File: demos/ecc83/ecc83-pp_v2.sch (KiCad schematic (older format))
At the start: 11 parts, among them P1 IN, P2 OUT, P3 POWER, P4 CONN_2, U1 ECC83

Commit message: Some demo files updated.
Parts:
- U1: value ECC83 -> ECC81_83
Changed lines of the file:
@@
-EESchema Schematic File Version 2  date 30/12/2010 18:27:52
-LIBS:power
-LIBS:device
-LIBS:valves
-LIBS:conn
-LIBS:linear
-LIBS:regul
-LIBS:74xx
-LIBS:cmos4000
-LIBS:adc-dac
-LIBS:memory
-LIBS:xilinx
-LIBS:special
-LIBS:microcontrollers
-LIBS:microchip
-LIBS:analog_switches
-LIBS:motorola
-LIBS:intel
-LIBS:audio
-LIBS:interface
-LIBS:digital-audio
-LIBS:philips
-LIBS:display
-LIBS:cypress
-LIBS:siliconi
-LIBS:contrib
-LIBS:ecc83-pp_v2-cache
-EELAYER 25  0
+EESchema Schematic File Version 2
+LIBS:power,device,valves,conn,linear,regul,74xx,cmos4000,adc-dac,memory,xilinx,special,microcontrollers,microchip,analog_switches,motorola,intel,audio,interface,digital-audio,philips,display,cypress,siliconi,contrib
+EELAYER 23  0
 EELAYER END
 $Descr A4 11700 8267
 Sheet 1 1
 Title "ECC Push-Pull"
-Date "30 dec 2010"
+Date "11 dec 2006"
 Rev "0.1"
 Comp ""
@@
 Wire Wire Line
 	5750 3850 5750 4050
+Connection ~ 4450 4500
 Wire Wire Line
 	4450 5400 4450 4450
@@
 U 3 1 48B4F266
 P 9950 5700
-F 0 "U1" H 10080 6010 50  0000 C CNN
-F 1 "ECC83" H 10300 5400 50  0000 C CNN
-F 2 "VALVE-NOVAL_P" H 10220 5300 50  0001 C CNN
+F 0 "U1" H 10080 6010 50  0000 C C
+F 1 "ECC81_83" H 10300 5400 50  0000 C C
+F 2 "VALVE-NOVAL_P" H 10220 5300 50  0001 C C
 	3    9950 5700
 	1    0    0    -1
@@
 U 2 1 48B4F263
 P 4950 4450
-F 0 "U1" H 5080 4760 50  0000 C CNN
-F 1 "ECC83" H 5150 4100 50  0000 C CNN
-F 2 "VALVE-NOVAL_P" H 5220 4050 50  0001 C CNN
+F 0 "U1" H 5080 4760 50  0000 C C
+F 1 "ECC83" H 5150 4100 50  0000 C C
+F 2 "VALVE-NOVAL_P" H 5220 4050 50  0001 C C
 	2    4950 4450
 	1    0    0    -1
@@
 U 1 1 48B4F256
 P 5750 4450
-F 0 "U1" H 5880 4760 50  0000 C CNN
-F 1 "ECC83" H 5500 4150 50  0000 C CNN
-F 2 "VALVE-NOVAL_P" H 6020 4050 50  0001 C CNN
+F 0 "U1" H 5880 4760 50  0000 C C
+F 1 "ECC83" H 5500 4150 50  0000 C C
+F 2 "VALVE-NOVAL_P" H 6020 4050 50  0001 C C
 	1    5750 4450
 	-1   0    0    -1
@@
 U 1 1 457DBAF8
 P 6950 5150
-F 0 "#PWR01" H 6950 5150 30  0001 C CNN
-F 1 "GND" H 6950 5080 30  0001 C CNN
+F 0 "#PWR01" H 6950 5150 30  0001 C C
+F 1 "GND" H 6950 5080 30  0001 C C
 	1    6950 5150
 	1    0    0    -1
@@
 U 1 1 457DBAF5
 P 6700 5900
-F 0 "#PWR02" H 6700 5900 30  0001 C CNN
-F 1 "GND" H 6700 5830 30  0001 C CNN
+F 0 "#PWR02" H 6700 5900 30  0001 C C
+F 1 "GND" H 6700 5830 30  0001 C C
 	1    6700 5900
 	1    0    0    -1
@@
 U 1 1 457DBAF1
 P 4850 5900
-F 0 "#PWR03" H 4850 5900 30  0001 C CNN
-F 1 "GND" H 4850 5830 30  0001 C CNN
+F 0 "#PWR03" H 4850 5900 30  0001 C C
+F 1 "GND" H 4850 5830 30  0001 C C
 	1    4850 5900
 	1    0    0    -1
@@
 U 1 1 457DBAEF
 P 4450 5900
-F 0 "#PWR04" H 4450 5900 30  0001 C CNN
-F 1 "GND" H 4450 5830 30  0001 C CNN
+F 0 "#PWR04" H 4450 5900 30  0001 C C
+F 1 "GND" H 4450 5830 30  0001 C C
 	1    4450 5900
 	1    0    0    -1
@@
 U 1 1 457DBAC0
 P 4100 5250
-F 0 "#FLG05" H 4100 5520 30  0001 C CNN
-F 1 "PWR_FLAG" H 4100 5480 30  0000 C CNN
+F 0 "#FLG05" H 4100 5520 30  0001 C C
+F 1 "PWR_FLAG" H 4100 5480 30  0000 C C
 	1    4100 5250
 	0    -1   -1   0
@@
 U 1 1 456A8ACC
 P 9950 6700
-F 0 "P4" V 9900 6700 40  0000 C CNN
-F 1 "CONN_2" V 10000 6700 40  0000 C CNN
+F 0 "P4" V 9900 6700 40  0000 C C
+F 1 "CONN_2" V 10000 6700 40  0000 C C
 	1    9950 6700
 	0    1    1    0
@@
 U 1 1 4549F4BE
 P 6700 4050
-F 0 "C1" H 6750 4150 50  0000 L CNN
-F 1 "10uF" H 6450 4150 50  0000 L CNN
+F 0 "C1" H 6750 4150 50  0000 L C
+F 1 "10uF" H 6450 4150 50  0000 L C
 	1    6700 4050
 	1    0    0    -1
@@
 U 1 1 4549F4B9
 P 4150 5300
-F 0 "#PWR06" H 4150 5300 30  0001 C CNN
-F 1 "GND" H 4150 5230 30  0001 C CNN
+F 0 "#PWR06" H 4150 5300 30  0001 C C
+F 1 "GND" H 4150 5230 30  0001 C C
 	1    4150 5300
 	1    0    0    -1
@@
 U 1 1 4549F4B3
 P 6950 4350
-F 0 "#PWR07" H 6950 4350 30  0001 C CNN
-F 1 "GND" H 6950 4280 30  0001 C CNN
+F 0 "#PWR07" H 6950 4350 30  0001 C C
+F 1 "GND" H 6950 4280 30  0001 C C
 	1    6950 4350
 	1    0    0    -1
@@
 U 1 1 4549F4A5
 P 7300 3950
-F 0 "P3" V 7250 3950 40  0000 C CNN
-F 1 "POWER" V 7350 3950 40  0000 C CNN
+F 0 "P3" V 7250 3950 40  0000 C C
+F 1 "POWER" V 7350 3950 40  0000 C C
 	1    7300 3950
 	1    0    0    -1
@@
 U 1 1 4549F46C
 P 7300 4900
-F 0 "P2" V 7250 4900 40  0000 C CNN
-F 1 "OUT" V 7350 4900 40  0000 C CNN
+F 0 "P2" V 7250 4900 40  0000 C C
+F 1 "OUT" V 7350 4900 40  0000 C C
 	1    7300 4900
 	1    0    0    -1
@@
 U 1 1 4549F464
 P 3800 4900
-F 0 "P1" V 3750 4900 40  0000 C CNN
-F 1 "IN" V 3850 4900 40  0000 C CNN
+F 0 "P1" V 3750 4900 40  0000 C C
+F 1 "IN" V 3850 4900 40  0000 C C
 	1    3800 4900
 	-1   0    0    1
@@
 U 1 1 4549F3BE
 P 6500 4800
-F 0 "C2" H 6550 4900 50  0000 L CNN
-F 1 "680nF" H 6550 4700 50  0000 L CNN
+F 0 "C2" H 6550 4900 50  0000 L C
+F 1 "680nF" H 6550 4700 50  0000 L C
 	1    6500 4800
 	0    1    1    0
@@
 U 1 1 4549F3AD
 P 6700 5650
-F 0 "R3" V 6780 5650 50  0000 C CNN
-F 1 "100K" V 6700 5650 50  0000 C CNN
+F 0 "R3" V 6780 5650 50  0000 C C
+F 1 "100K" V 6700 5650 50  0000 C C
 	1    6700 5650
 	1    0    0    -1
@@
 U 1 1 4549F3A2
 P 4450 5650
-F 0 "R4" V 4530 5650 50  0000 C CNN
-F 1 "47K" V 4450 5650 50  0000 C CNN
+F 0 "R4" V 4530 5650 50  0000 C C
+F 1 "47K" V 4450 5650 50  0000 C C
 	1    4450 5650
 	1    0    0    -1
@@
 U 1 1 4549F39D
 P 4850 5650
-F 0 "R2" V 4930 5650 50  0000 C CNN
-F 1 "1.5K" V 4850 5650 50  0000 C CNN
+F 0 "R2" V 4930 5650 50  0000 C C
+F 1 "1.5K" V 4850 5650 50  0000 C C
 	1    4850 5650
 	1    0    0    -1
@@
 U 1 1 4549F38A
 P 6300 4250
-F 0 "R1" V 6380 4250 50  0000 C CNN
-F 1 "1.5K" V 6300 4250 50  0000 C CNN
+F 0 "R1" V 6380 4250 50  0000 C C
+F 1 "1.5K" V 6300 4250 50  0000 C C
 	1    6300 4250
 	1    0    0    -1

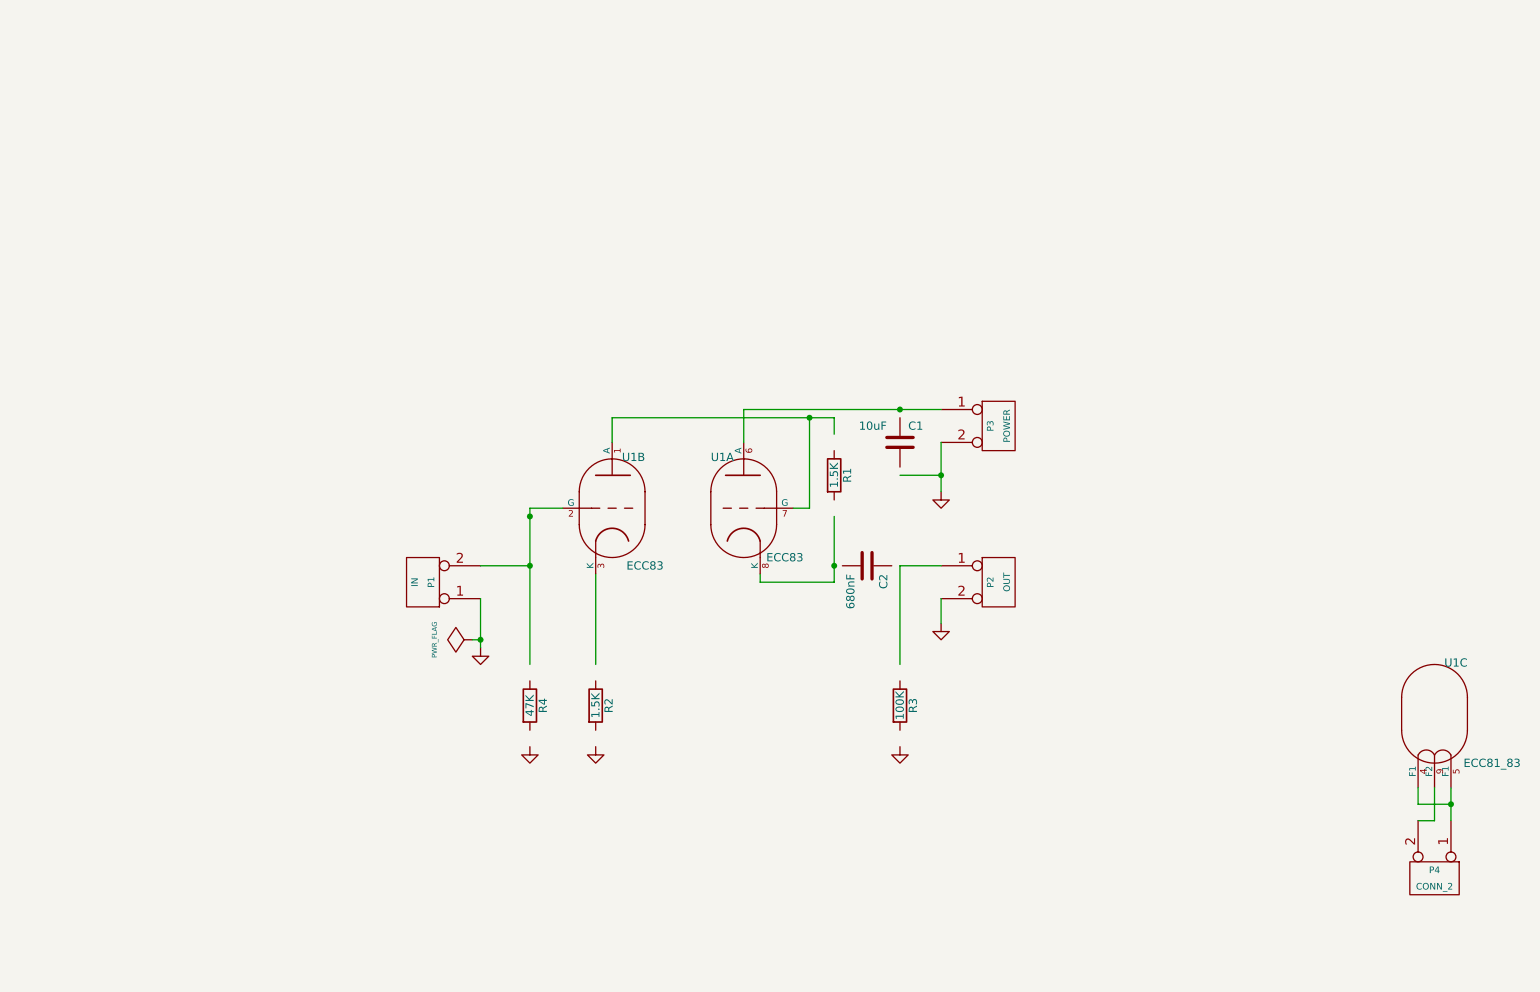
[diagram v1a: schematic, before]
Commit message: Update old demo board files. Minor code cleaning.
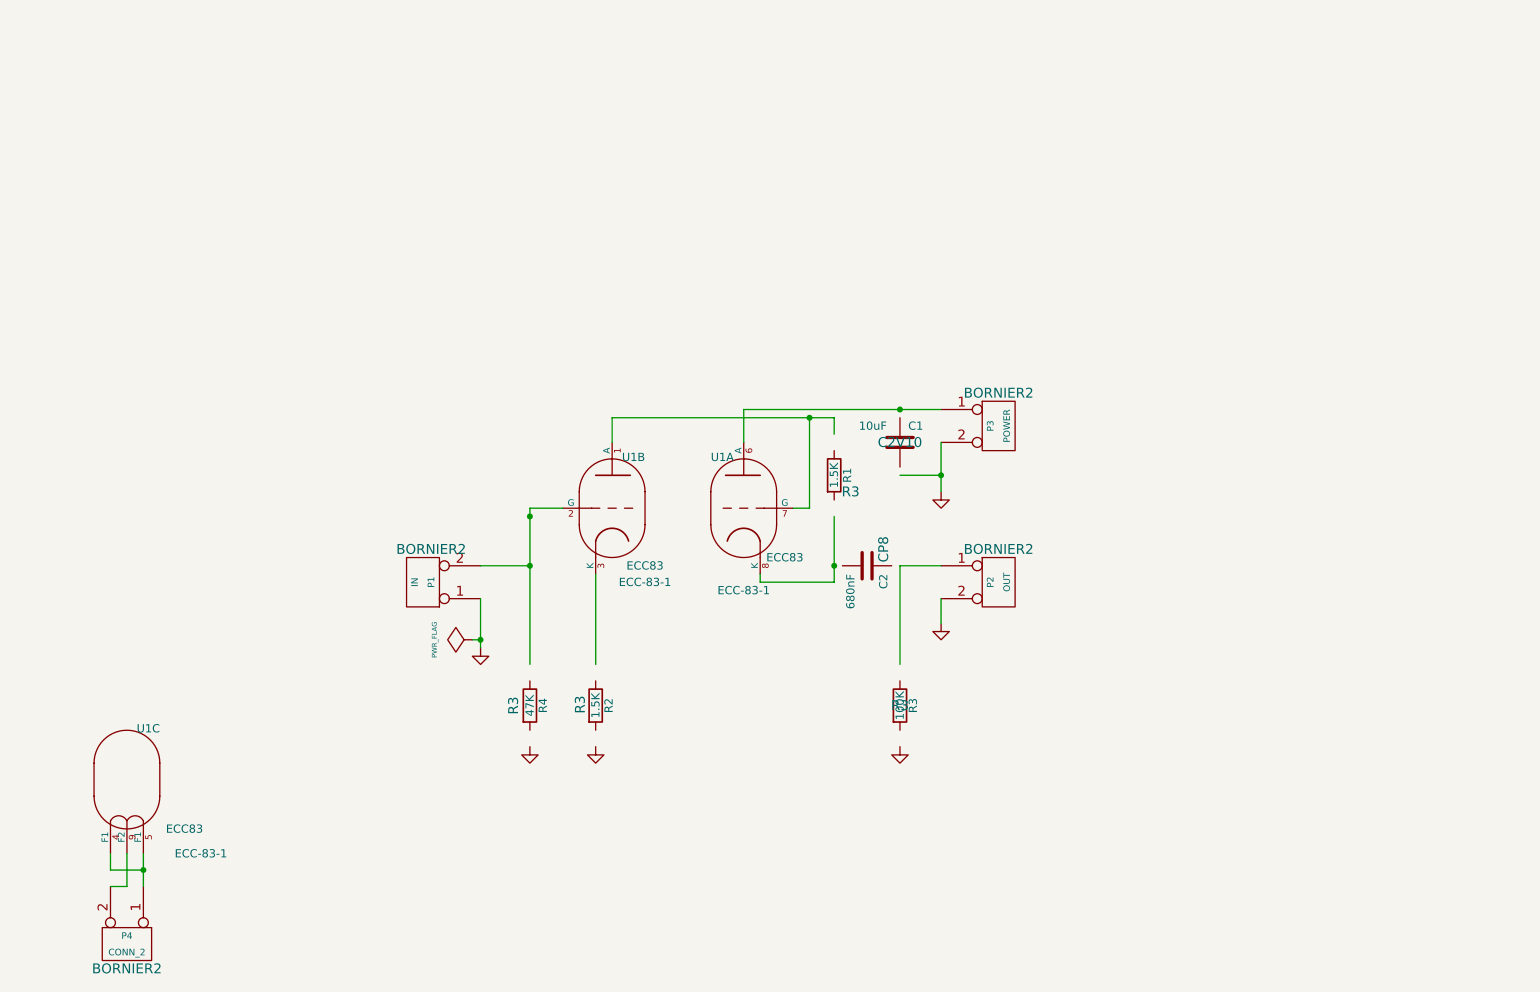
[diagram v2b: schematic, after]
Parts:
- C1: footprint (none) -> C2V10
- C2: footprint (none) -> CP8
- P1, P2, P3, P4: footprint (none) -> BORNIER2
- R1, R2, R3, R4: footprint (none) -> R3
- U1: footprint VALVE-NOVAL_P -> ECC-83-1
- U1: value ECC81_83 -> ECC83; footprint VALVE-NOVAL_P -> ECC-83-1
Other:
- moved on the sheet: P4, U1C
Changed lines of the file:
@@
 EESchema Schematic File Version 2
-LIBS:power,device,valves,conn,linear,regul,74xx,cmos4000,adc-dac,memory,xilinx,special,microcontrollers,microchip,analog_switches,motorola,intel,audio,interface,digital-audio,philips,display,cypress,siliconi,contrib
-EELAYER 23  0
+LIBS:power
+LIBS:device
+LIBS:valves
+LIBS:conn
+LIBS:linear
+LIBS:regul
+LIBS:74xx
+LIBS:cmos4000
+LIBS:adc-dac
+LIBS:memory
+LIBS:xilinx
+LIBS:special
+LIBS:microcontrollers
+LIBS:microchip
+LIBS:analog_switches
+LIBS:motorola
+LIBS:intel
+LIBS:audio
+LIBS:interface
+LIBS:digital-audio
+LIBS:philips
+LIBS:display
+LIBS:cypress
+LIBS:siliconi
+LIBS:contrib
+LIBS:ecc83-pp_v2-cache
+EELAYER 24 0
 EELAYER END
-$Descr A4 11700 8267
+$Descr A4 11693 8268
+encoding utf-8
 Sheet 1 1
 Title "ECC Push-Pull"
@@
 	4450 4450 4650 4450
 Wire Wire Line
-	9850 6350 9950 6350
-Wire Wire Line
-	9950 6350 9950 6150
+	1900 6750 2000 6750
+Wire Wire Line
+	2000 6750 2000 6550
 Wire Wire Line
 	4150 5300 4150 5000
@@
 	6700 4800 6700 5400
 Wire Wire Line
-	10050 6150 10050 6350
-Wire Wire Line
-	10050 6250 9850 6250
-Connection ~ 10050 6250
+	2100 6550 2100 6750
+Wire Wire Line
+	2100 6650 1900 6650
+Connection ~ 2100 6650
 Wire Wire Line
 	4100 5250 4150 5250
 Connection ~ 4150 5250
 Wire Wire Line
-	9850 6250 9850 6150
+	1900 6650 1900 6550
 Wire Wire Line
 	6300 3900 4950 3900
@@
 L ECC83 U1
 U 3 1 48B4F266
-P 9950 5700
-F 0 "U1" H 10080 6010 50  0000 C C
-F 1 "ECC81_83" H 10300 5400 50  0000 C C
-F 2 "VALVE-NOVAL_P" H 10220 5300 50  0001 C C
-	3    9950 5700
+P 2000 6100
+F 0 "U1" H 2130 6410 50  0000 C CNN
+F 1 "ECC83" H 2350 5800 50  0000 C CNN
+F 2 "ECC-83-1" H 2450 5650 50  0000 C CNN
+F 3 "" H 2000 6100 60  0001 C CNN
+	3    2000 6100
 	1    0    0    -1
 $EndComp
@@
 U 2 1 48B4F263
 P 4950 4450
-F 0 "U1" H 5080 4760 50  0000 C C
-F 1 "ECC83" H 5150 4100 50  0000 C C
-F 2 "VALVE-NOVAL_P" H 5220 4050 50  0001 C C
+F 0 "U1" H 5080 4760 50  0000 C CNN
+F 1 "ECC83" H 5150 4100 50  0000 C CNN
+F 2 "ECC-83-1" H 5150 4000 50  0000 C CNN
+F 3 "" H 4950 4450 60  0001 C CNN
 	2    4950 4450
 	1    0    0    -1
@@
 U 1 1 48B4F256
 P 5750 4450
-F 0 "U1" H 5880 4760 50  0000 C C
-F 1 "ECC83" H 5500 4150 50  0000 C C
-F 2 "VALVE-NOVAL_P" H 6020 4050 50  0001 C C
+F 0 "U1" H 5880 4760 50  0000 C CNN
+F 1 "ECC83" H 5500 4150 50  0000 C CNN
+F 2 "ECC-83-1" H 5750 3950 50  0000 C CNN
+F 3 "" H 5750 4450 60  0001 C CNN
 	1    5750 4450
 	-1   0    0    -1
@@
 U 1 1 457DBAF8
 P 6950 5150
-F 0 "#PWR01" H 6950 5150 30  0001 C C
-F 1 "GND" H 6950 5080 30  0001 C C
+F 0 "#PWR01" H 6950 5150 30  0001 C CNN
+F 1 "GND" H 6950 5080 30  0001 C CNN
+F 2 "" H 6950 5150 60  0001 C CNN
+F 3 "" H 6950 5150 60  0001 C CNN
 	1    6950 5150
 	1    0    0    -1
@@
 U 1 1 457DBAF5
 P 6700 5900
-F 0 "#PWR02" H 6700 5900 30  0001 C C
-F 1 "GND" H 6700 5830 30  0001 C C
+F 0 "#PWR02" H 6700 5900 30  0001 C CNN
+F 1 "GND" H 6700 5830 30  0001 C CNN
+F 2 "" H 6700 5900 60  0001 C CNN
+F 3 "" H 6700 5900 60  0001 C CNN
 	1    6700 5900
 	1    0    0    -1
@@
 U 1 1 457DBAF1
 P 4850 5900
-F 0 "#PWR03" H 4850 5900 30  0001 C C
-F 1 "GND" H 4850 5830 30  0001 C C
+F 0 "#PWR03" H 4850 5900 30  0001 C CNN
+F 1 "GND" H 4850 5830 30  0001 C CNN
+F 2 "" H 4850 5900 60  0001 C CNN
+F 3 "" H 4850 5900 60  0001 C CNN
 	1    4850 5900
 	1    0    0    -1
@@
 U 1 1 457DBAEF
 P 4450 5900
-F 0 "#PWR04" H 4450 5900 30  0001 C C
-F 1 "GND" H 4450 5830 30  0001 C C
+F 0 "#PWR04" H 4450 5900 30  0001 C CNN
+F 1 "GND" H 4450 5830 30  0001 C CNN
+F 2 "" H 4450 5900 60  0001 C CNN
+F 3 "" H 4450 5900 60  0001 C CNN
 	1    4450 5900
 	1    0    0    -1
@@
 U 1 1 457DBAC0
 P 4100 5250
-F 0 "#FLG05" H 4100 5520 30  0001 C C
-F 1 "PWR_FLAG" H 4100 5480 30  0000 C C
+F 0 "#FLG05" H 4100 5520 30  0001 C CNN
+F 1 "PWR_FLAG" H 4100 5480 30  0000 C CNN
+F 2 "" H 4100 5250 60  0001 C CNN
+F 3 "" H 4100 5250 60  0001 C CNN
 	1    4100 5250
 	0    -1   -1   0
@@
 L CONN_2 P4
 U 1 1 456A8ACC
-P 9950 6700
-F 0 "P4" V 9900 6700 40  0000 C C
-F 1 "CONN_2" V 10000 6700 40  0000 C C
-	1    9950 6700
+P 2000 7100
+F 0 "P4" V 1950 7100 40  0000 C CNN
+F 1 "CONN_2" V 2050 7100 40  0000 C CNN
+F 2 "BORNIER2" V 2150 7100 60  0000 C CNN
+F 3 "" H 2000 7100 60  0001 C CNN
+	1    2000 7100
 	0    1    1    0
 $EndComp
@@
 U 1 1 4549F4BE
 P 6700 4050
-F 0 "C1" H 6750 4150 50  0000 L C
-F 1 "10uF" H 6450 4150 50  0000 L C
+F 0 "C1" H 6750 4150 50  0000 L CNN
+F 1 "10uF" H 6450 4150 50  0000 L CNN
+F 2 "C2V10" H 6700 4050 60  0000 C CNN
+F 3 "" H 6700 4050 60  0001 C CNN
 	1    6700 4050
 	1    0    0    -1
@@
 U 1 1 4549F4B9
 P 4150 5300
-F 0 "#PWR06" H 4150 5300 30  0001 C C
-F 1 "GND" H 4150 5230 30  0001 C C
+F 0 "#PWR06" H 4150 5300 30  0001 C CNN
+F 1 "GND" H 4150 5230 30  0001 C CNN
+F 2 "" H 4150 5300 60  0001 C CNN
+F 3 "" H 4150 5300 60  0001 C CNN
 	1    4150 5300
 	1    0    0    -1
@@
 U 1 1 4549F4B3
 P 6950 4350
-F 0 "#PWR07" H 6950 4350 30  0001 C C
-F 1 "GND" H 6950 4280 30  0001 C C
+F 0 "#PWR07" H 6950 4350 30  0001 C CNN
+F 1 "GND" H 6950 4280 30  0001 C CNN
+F 2 "" H 6950 4350 60  0001 C CNN
+F 3 "" H 6950 4350 60  0001 C CNN
 	1    6950 4350
 	1    0    0    -1
@@
 U 1 1 4549F4A5
 P 7300 3950
-F 0 "P3" V 7250 3950 40  0000 C C
-F 1 "POWER" V 7350 3950 40  0000 C C
+F 0 "P3" V 7250 3950 40  0000 C CNN
+F 1 "POWER" V 7350 3950 40  0000 C CNN
+F 2 "BORNIER2" H 7300 4150 60  0000 C CNN
+F 3 "" H 7300 3950 60  0001 C CNN
 	1    7300 3950
 	1    0    0    -1
@@
 U 1 1 4549F46C
 P 7300 4900
-F 0 "P2" V 7250 4900 40  0000 C C
-F 1 "OUT" V 7350 4900 40  0000 C C
+F 0 "P2" V 7250 4900 40  0000 C CNN
+F 1 "OUT" V 7350 4900 40  0000 C CNN
+F 2 "BORNIER2" H 7300 5100 60  0000 C CNN
+F 3 "" H 7300 4900 60  0001 C CNN
 	1    7300 4900
 	1    0    0    -1
@@
 U 1 1 4549F464
 P 3800 4900
-F 0 "P1" V 3750 4900 40  0000 C C
-F 1 "IN" V 3850 4900 40  0000 C C
+F 0 "P1" V 3750 4900 40  0000 C CNN
+F 1 "IN" V 3850 4900 40  0000 C CNN
+F 2 "BORNIER2" H 3750 4700 60  0000 C CNN
+F 3 "" H 3800 4900 60  0001 C CNN
 	1    3800 4900
 	-1   0    0    1
@@
 U 1 1 4549F3BE
 P 6500 4800
-F 0 "C2" H 6550 4900 50  0000 L C
-F 1 "680nF" H 6550 4700 50  0000 L C
+F 0 "C2" H 6550 4900 50  0000 L CNN
+F 1 "680nF" H 6550 4700 50  0000 L CNN
+F 2 "CP8" H 6400 4900 60  0000 C CNN
+F 3 "" H 6500 4800 60  0001 C CNN
 	1    6500 4800
 	0    1    1    0
@@
 U 1 1 4549F3AD
 P 6700 5650
-F 0 "R3" V 6780 5650 50  0000 C C
-F 1 "100K" V 6700 5650 50  0000 C C
+F 0 "R3" V 6780 5650 50  0000 C CNN
+F 1 "100K" V 6700 5650 50  0000 C CNN
+F 2 "R3" H 6700 5650 60  0000 C CNN
+F 3 "" H 6700 5650 60  0001 C CNN
 	1    6700 5650
 	1    0    0    -1
@@
 U 1 1 4549F3A2
 P 4450 5650
-F 0 "R4" V 4530 5650 50  0000 C C
-F 1 "47K" V 4450 5650 50  0000 C C
+F 0 "R4" V 4530 5650 50  0000 C CNN
+F 1 "47K" V 4450 5650 50  0000 C CNN
+F 2 "R3" V 4350 5650 60  0000 C CNN
+F 3 "" H 4450 5650 60  0001 C CNN
 	1    4450 5650
 	1    0    0    -1
@@
 U 1 1 4549F39D
 P 4850 5650
-F 0 "R2" V 4930 5650 50  0000 C C
-F 1 "1.5K" V 4850 5650 50  0000 C C
+F 0 "R2" V 4930 5650 50  0000 C CNN
+F 1 "1.5K" V 4850 5650 50  0000 C CNN
+F 2 "R3" V 4756 5656 60  0000 C CNN
+F 3 "" H 4850 5650 60  0001 C CNN
 	1    4850 5650
 	1    0    0    -1
@@
 U 1 1 4549F38A
 P 6300 4250
-F 0 "R1" V 6380 4250 50  0000 C C
-F 1 "1.5K" V 6300 4250 50  0000 C C
+F 0 "R1" V 6380 4250 50  0000 C CNN
+F 1 "1.5K" V 6300 4250 50  0000 C CNN
+F 2 "R3" H 6400 4150 60  0000 C CNN
+F 3 "" H 6300 4250 60  0001 C CNN
 	1    6300 4250
 	1    0    0    -1
